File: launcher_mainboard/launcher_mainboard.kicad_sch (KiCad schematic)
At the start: 82 parts, among them J1 USB_C_Receptacle_USB2.0_16P, J10 header, J11 header, J2 Conn_01x06, J3 Conn_01x06, J4 Conn_01x06, J5 Conn_01x06, J6 bat_con, J7 fan_con, J8 ESC_1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

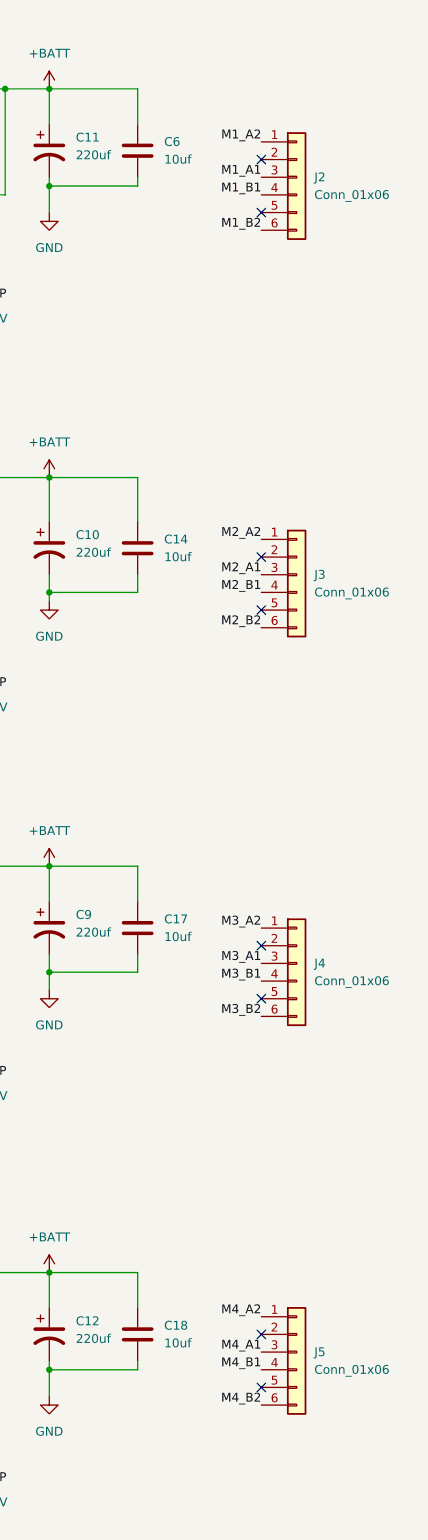
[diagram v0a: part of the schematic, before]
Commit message: switch stepper connector to XH
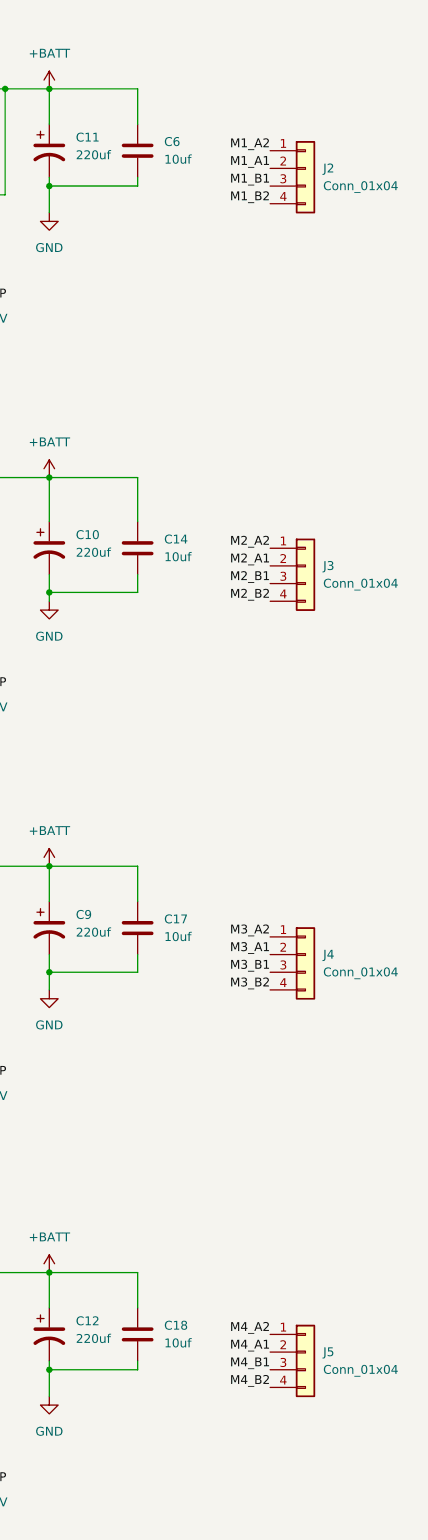
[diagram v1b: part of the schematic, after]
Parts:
- removed J2, J3, J4, J5: Conn_01x06, Connector_JST:JST_PH_B6B-PH-K_1x06_P2.00mm_Vertical, symbol Connector_Generic:Conn_01x06
- added J2, J3, J4, J5: Conn_01x04, Connector_JST:JST_XH_B4B-XH-A_1x04_P2.50mm_Vertical, symbol Connector_Generic:Conn_01x04
- C10, C11, C12, C9: footprint Capacitor_SMD:CP_Elec_8x10.5 -> Capacitor_SMD:CP_Elec_8x6.7
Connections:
- net M1_A1: now also J2.2 (Pin_2)
- net M1_A2: now also J2.1 (Pin_1)
- net M1_B1: now also J2.3 (Pin_3)
- net M1_B2: now also J2.4 (Pin_4)
- net M2_A1: now also J3.2 (Pin_2)
- net M2_A2: now also J3.1 (Pin_1)
- net M2_B1: now also J3.3 (Pin_3)
- net M2_B2: now also J3.4 (Pin_4)
- net M3_A1: now also J4.2 (Pin_2)
- net M3_A2: now also J4.1 (Pin_1)
- net M3_B1: now also J4.3 (Pin_3)
- net M3_B2: now also J4.4 (Pin_4)
- net M4_A1: now also J5.2 (Pin_2)
- net M4_A2: now also J5.1 (Pin_1)
- net M4_B1: now also J5.3 (Pin_3)
- net M4_B2: now also J5.4 (Pin_4)
- no-connect marks 64 -> 56

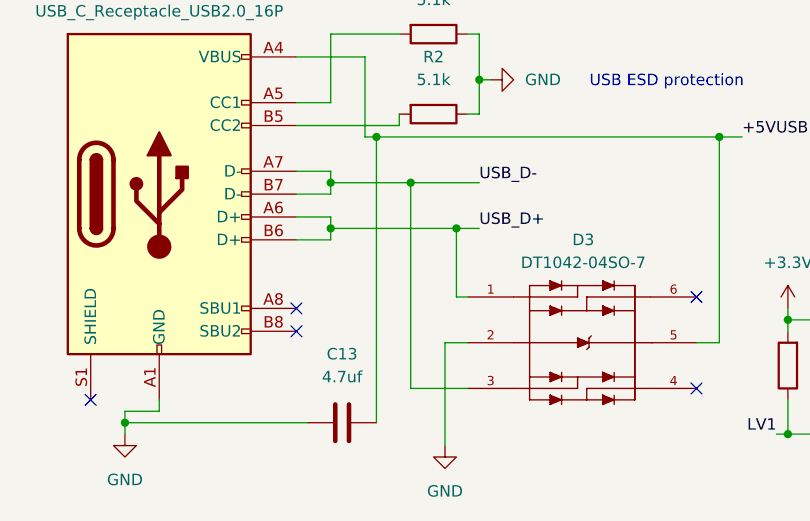
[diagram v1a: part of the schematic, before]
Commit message: flipped ESD IC, selected zener diode and updated footprint
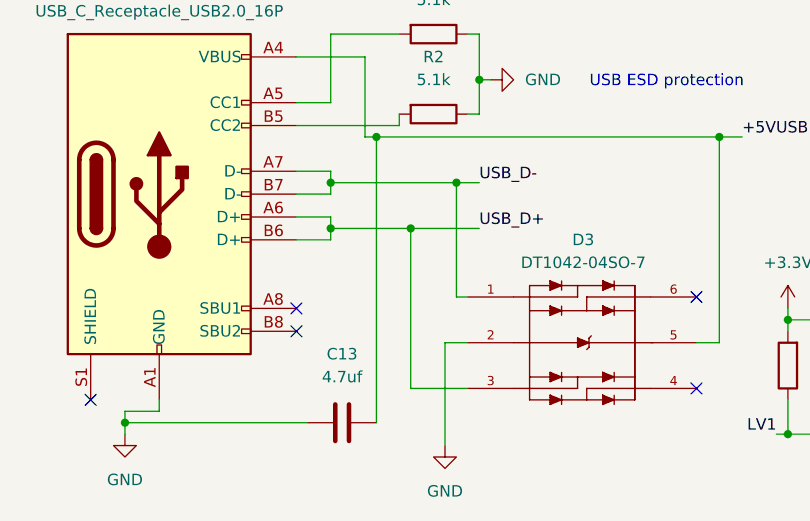
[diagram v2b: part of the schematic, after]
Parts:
- D2: footprint Diode_SMD:D_0805_2012Metric -> Diode_SMD:D_SOD-123
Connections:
- net USB_D+: now also D3.3; no longer D3.1
- net USB_D-: now also D3.1; no longer D3.3
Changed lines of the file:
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@@
 	)
 	(junction
+		(at 67.31 238.76)
+		(diameter 0)
+		(color 0 0 0 0)
+	)
+	(junction
 		(at 104.14 254)
 		(diameter 0)
@@
 	)
 	(junction
-		(at 62.23 238.76)
-		(diameter 0)
-		(color 0 0 0 0)
-	)
-	(junction
 		(at 355.6 29.21)
 		(diameter 0)
@@
 	)
 	(junction
-		(at 67.31 243.84)
-		(diameter 0)
-		(color 0 0 0 0)
-	)
-	(junction
 		(at 207.01 137.16)
 		(diameter 0)
@@
 	)
 	(junction
+		(at 62.23 243.84)
+		(diameter 0)
+		(color 0 0 0 0)
+	)
+	(junction
 		(at 48.26 182.88)
 		(diameter 0)
@@
 	(wire
 		(pts
-			(xy 53.34 238.76) (xy 62.23 238.76)
+			(xy 53.34 238.76) (xy 67.31 238.76)
 		)
 		(stroke
@@
 	(wire
 		(pts
-			(xy 53.34 243.84) (xy 67.31 243.84)
+			(xy 53.34 243.84) (xy 62.23 243.84)
 		)
 		(stroke
@@
 	(wire
 		(pts
-			(xy 67.31 243.84) (xy 67.31 251.46)
-		)
-		(stroke
-			(width 0)
-			(type default)
-		)
-	)
-	(wire
-		(pts
 			(xy 101.6 72.39) (xy 100.33 72.39)
 		)
@@
 	(wire
 		(pts
+			(xy 67.31 238.76) (xy 69.85 238.76)
+		)
+		(stroke
+			(width 0)
+			(type default)
+		)
+	)
+	(wire
+		(pts
 			(xy 49.53 232.41) (xy 60.96 232.41)
 		)
@@
 	(wire
 		(pts
-			(xy 67.31 243.84) (xy 69.85 243.84)
-		)
-		(stroke
-			(width 0)
-			(type default)
-		)
-	)
-	(wire
-		(pts
 			(xy 161.29 252.73) (xy 161.29 255.27)
 		)
@@
 	(wire
 		(pts
-			(xy 62.23 261.62) (xy 62.23 238.76)
-		)
-		(stroke
-			(width 0)
-			(type default)
-		)
-	)
-	(wire
-		(pts
 			(xy 68.58 82.55) (xy 69.85 82.55)
 		)
@@
 	(wire
 		(pts
+			(xy 62.23 243.84) (xy 69.85 243.84)
+		)
+		(stroke
+			(width 0)
+			(type default)
+		)
+	)
+	(wire
+		(pts
 			(xy 355.6 85.09) (xy 368.3 85.09)
 		)
@@
 	(wire
 		(pts
+			(xy 62.23 243.84) (xy 62.23 261.62)
+		)
+		(stroke
+			(width 0)
+			(type default)
+		)
+	)
+	(wire
+		(pts
 			(xy 281.94 217.17) (xy 289.56 217.17)
 		)
@@
 	(wire
 		(pts
-			(xy 62.23 238.76) (xy 69.85 238.76)
+			(xy 30.48 264.16) (xy 30.48 265.43)
 		)
 		(stroke
@@
 	(wire
 		(pts
-			(xy 30.48 264.16) (xy 30.48 265.43)
+			(xy 123.19 252.73) (xy 123.19 255.27)
 		)
 		(stroke
@@
 	(wire
 		(pts
-			(xy 123.19 252.73) (xy 123.19 255.27)
+			(xy 191.77 147.32) (xy 191.77 152.4)
 		)
 		(stroke
@@
 	(wire
 		(pts
-			(xy 191.77 147.32) (xy 191.77 152.4)
+			(xy 355.6 29.21) (xy 355.6 34.29)
 		)
 		(stroke
@@
 	(wire
 		(pts
-			(xy 355.6 29.21) (xy 355.6 34.29)
+			(xy 201.93 200.66) (xy 201.93 203.2)
 		)
 		(stroke
@@
 	(wire
 		(pts
-			(xy 201.93 200.66) (xy 201.93 203.2)
+			(xy 215.9 262.89) (xy 215.9 266.7)
 		)
 		(stroke
@@
 	(wire
 		(pts
-			(xy 215.9 262.89) (xy 215.9 266.7)
+			(xy 67.31 238.76) (xy 67.31 251.46)
 		)
 		(stroke
@@
 			)
 		)
-		(property "Footprint" "Diode_SMD:D_0805_2012Metric"
+		(property "Footprint" "Diode_SMD:D_SOD-123"
 			(at 68.58 146.05 0)
 			(effects

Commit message: finished up diode stuff
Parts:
- D1: value POWER_LED -> GREEN_LED
- D4: value INDICATOR_LED_1 -> RED_LED_1
- D5: value INDICATOR_LED_2 -> BLUE_LED_2
- D6: value 1N4004 -> SD103AW-TP; footprint Diode_SMD:D_0805_2012Metric -> Diode_SMD:D_SOD-123
- R10, R3: value 200 -> 100
- R12: value 200 -> 20
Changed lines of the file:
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@@
 			)
 		)
-		(property "Value" "INDICATOR_LED_1"
+		(property "Value" "RED_LED_1"
 			(at 175.26 95.5674 90)
 			(effects
@@
 			)
 		)
-		(property "Value" "200"
+		(property "Value" "20"
 			(at 210.82 85.09 90)
 			(effects
@@
 			)
 		)
-		(property "Value" "200"
+		(property "Value" "100"
 			(at 157.48 83.82 90)
 			(effects
@@
 			)
 		)
-		(property "Value" "INDICATOR_LED_2"
+		(property "Value" "BLUE_LED_2"
 			(at 228.6 96.8374 90)
 			(effects
@@
 			)
 		)
-		(property "Value" "200"
+		(property "Value" "100"
 			(at 260.35 54.6099 0)
 			(effects
@@
 			)
 		)
-		(property "Value" "1N4004"
+		(property "Value" "SD103AW-TP"
 			(at 137.16 31.242 90)
 			(effects
@@
 			)
 		)
-		(property "Footprint" "Diode_SMD:D_0805_2012Metric"
+		(property "Footprint" "Diode_SMD:D_SOD-123"
 			(at 142.875 30.48 0)
 			(effects
@@
 			)
 		)
-		(property "Value" "POWER_LED"
+		(property "Value" "GREEN_LED"
 			(at 252.73 63.5 0)
 			(effects

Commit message: ordered board
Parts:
- R7: value 4k -> 3.9k
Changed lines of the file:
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@@
 			)
 		)
-		(property "Value" "4k"
+		(property "Value" "3.9k"
 			(at 77.47 133.35 90)
 			(effects
